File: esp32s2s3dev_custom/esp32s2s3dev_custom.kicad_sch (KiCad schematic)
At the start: 33 parts, among them J1 Vin, J2 Vout, U1 ESP32-S3-DevKitC, U3 R-78E3.3-0.5, U4 L7805

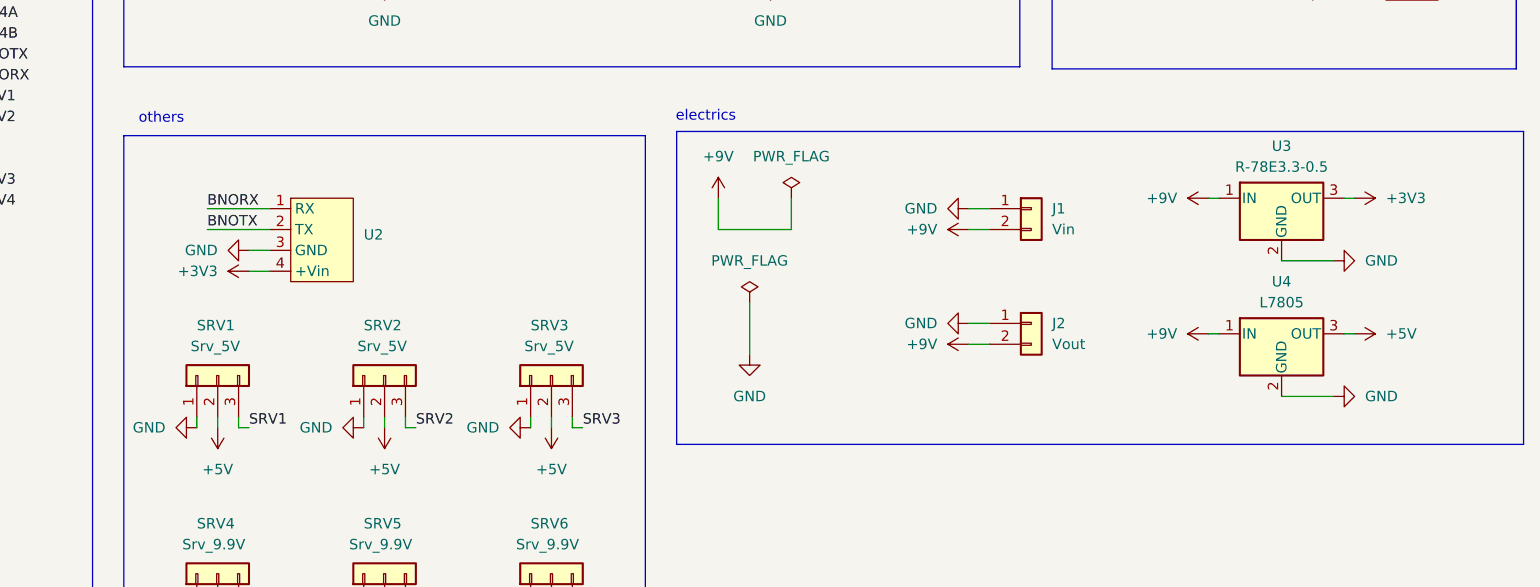
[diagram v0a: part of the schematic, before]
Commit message: add capacitor to registor, regulator to BNO serial
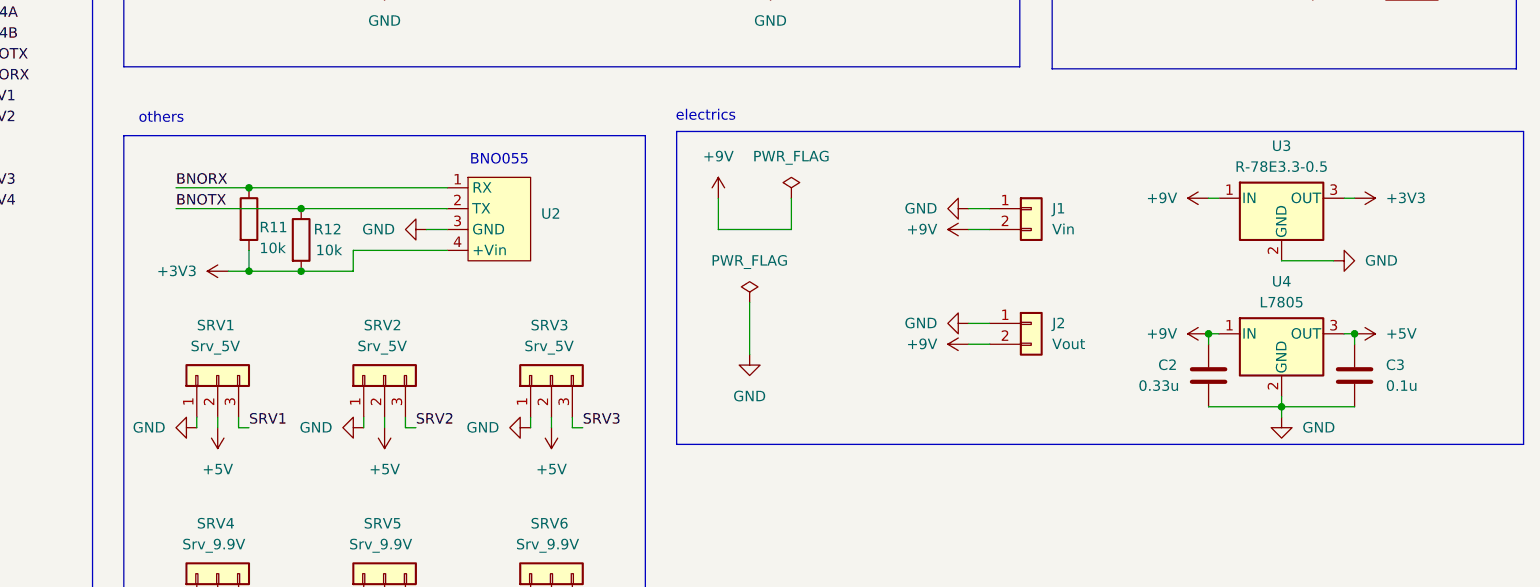
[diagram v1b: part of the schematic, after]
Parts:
- added C2: 0.33u, Capacitor_THT:C_Disc_D3.0mm_W1.6mm_P2.50mm, symbol Device:C
- added C3: 0.1u, Capacitor_THT:C_Disc_D3.0mm_W1.6mm_P2.50mm, symbol Device:C
- added R11, R12: 10k, Resistor_THT:R_Axial_DIN0204_L3.6mm_D1.6mm_P5.08mm_Horizontal, symbol Device:R
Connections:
- net +3V3: now also R11.2, R12.2
- net +5V: now also C3.1
- net +9V: now also C2.2
- net BNORX: now also R11.1
- net BNOTX: now also R12.1
- net GND: now also C2.1, C3.2
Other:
- note added: "BNO055"
- moved on the sheet: U2
